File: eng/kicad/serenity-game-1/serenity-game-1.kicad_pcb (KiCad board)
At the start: 2 copper layers, 9 parts, among them U1 PIC16F690-IP

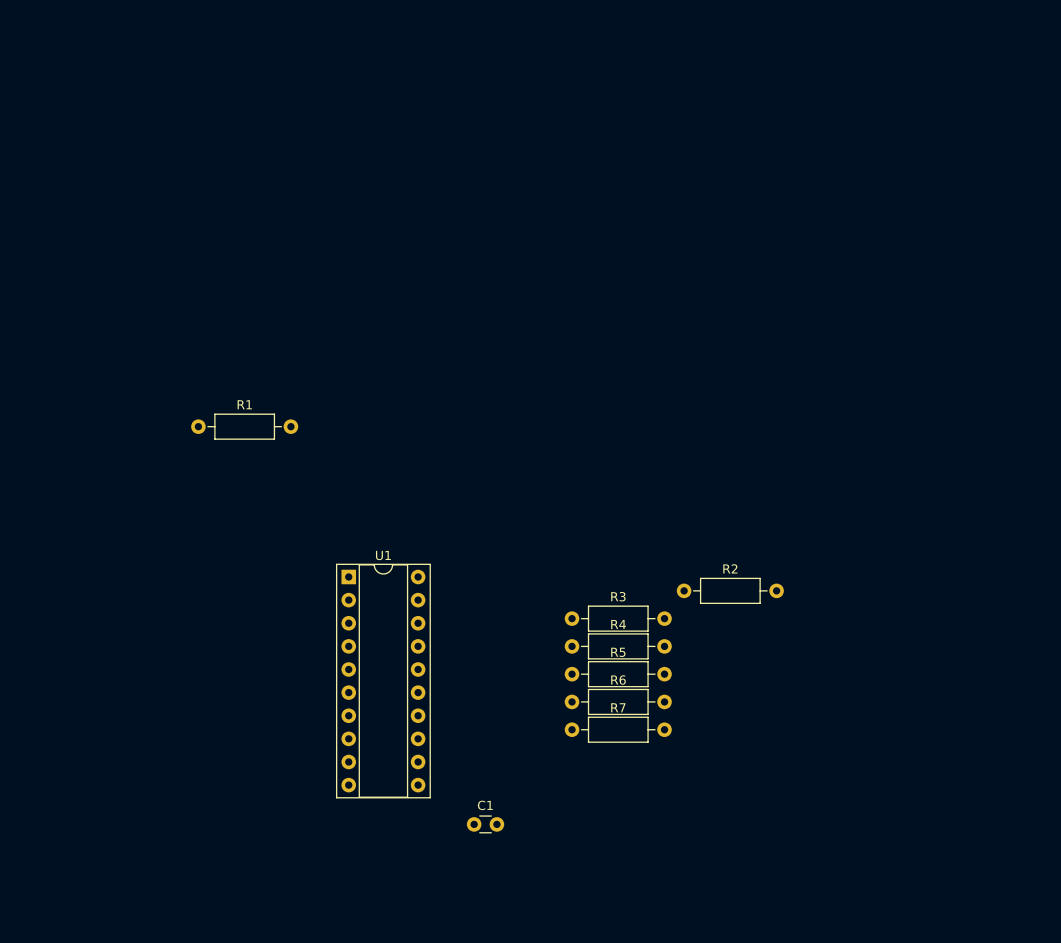
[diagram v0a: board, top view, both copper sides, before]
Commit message: Schematic addition of buttons and labeling of wires (WIP).
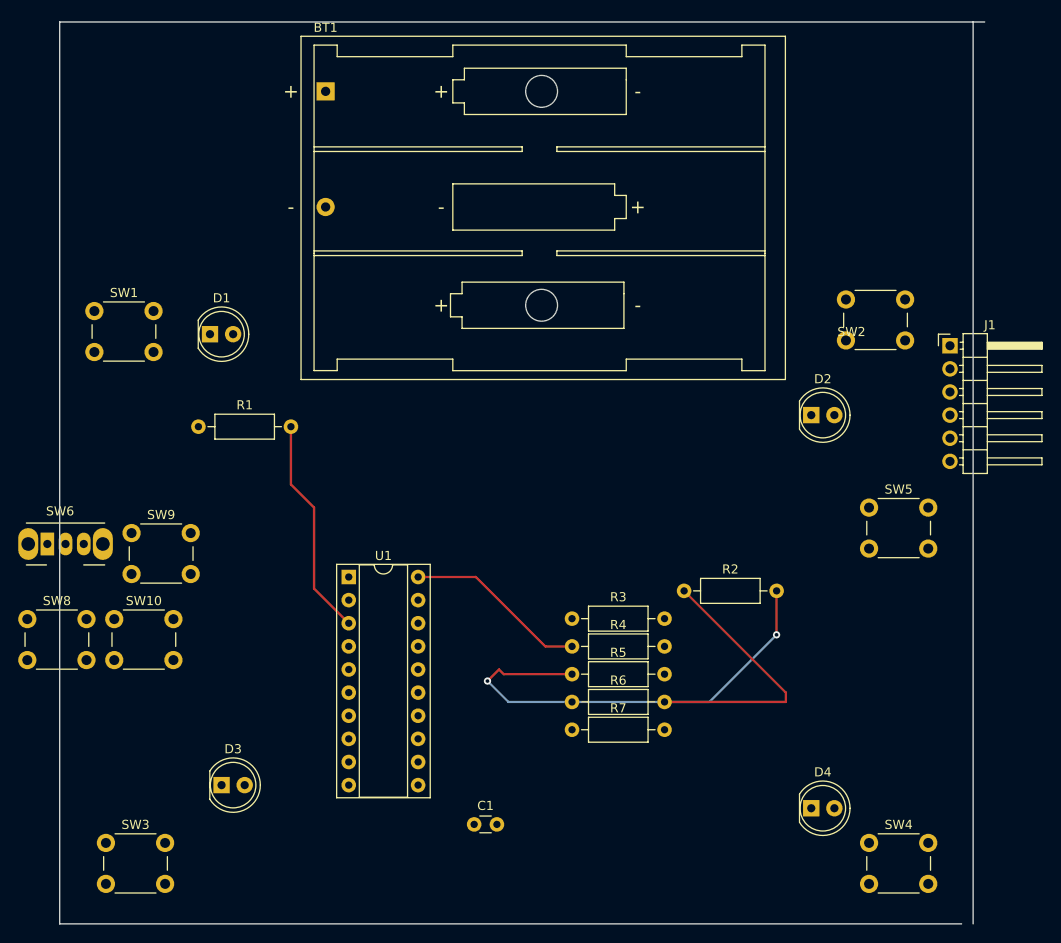
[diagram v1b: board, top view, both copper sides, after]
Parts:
- added BT1: Battery, Battery:BatteryHolder_Keystone_2479_3xAAA, F.Cu at (111.8, 26.7)
- added D1: LED, LED_THT:LED_D5.0mm, F.Cu at (99.1, 53.3)
- added D2: LED, LED_THT:LED_D5.0mm, F.Cu at (165.1, 62.2)
- added D3: LED, LED_THT:LED_D5.0mm, F.Cu at (100.3, 102.9)
- added D4: LED, LED_THT:LED_D5.0mm, F.Cu at (165.1, 105.4)
- added J1: Conn_01x06_Male, Connector_PinHeader_2.54mm:PinHeader_1x06_P2.54mm_Horizontal, F.Cu at (180.3, 54.6)
- added SW1: SW_Push, Button_Switch_THT:SW_PUSH_6mm_H7.3mm, F.Cu at (86.4, 50.8)
- added SW10: SW_Push, Button_Switch_THT:SW_PUSH_6mm_H7.3mm, F.Cu at (88.5, 84.6)
- added SW2: SW_Push, Button_Switch_THT:SW_PUSH_6mm_H7.3mm, F.Cu at (168.9, 49.5)
- added SW3: SW_Push, Button_Switch_THT:SW_PUSH_6mm_H7.3mm, F.Cu at (87.6, 109.2)
- added SW4: SW_Push, Button_Switch_THT:SW_PUSH_6mm_H7.3mm, F.Cu at (171.4, 109.2)
- added SW5: SW_Push, Button_Switch_THT:SW_PUSH_6mm_H7.3mm, F.Cu at (171.4, 72.4)
- added SW6: SW_SPDT, Button_Switch_THT:SW_CuK_OS102011MA1QN1_SPDT_Angled, F.Cu at (81.2, 76.4)
- added SW8: SW_Push, Button_Switch_THT:SW_PUSH_6mm_H7.3mm, F.Cu at (79.0, 84.6)
- added SW9: SW_Push, Button_Switch_THT:SW_PUSH_6mm_H7.3mm, F.Cu at (90.4, 75.2)
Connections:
- C1 pad 1: (no net) -> Net-(C1-Pad1)
- C1 pad 2: (no net) -> Net-(C1-Pad2)
- R1 pad 1: (no net) -> Net-(R1-Pad1)
- R1 pad 2: (no net) -> Net-(R1-Pad2)
- R2 pad 1: (no net) -> Net-(R2-Pad1)
- R2 pad 2: (no net) -> Net-(R2-Pad2)
- R3 pad 1: (no net) -> Net-(R3-Pad1)
- R3 pad 2: (no net) -> Net-(R3-Pad2)
- R4 pad 1: (no net) -> Net-(R4-Pad1)
- R4 pad 2: (no net) -> Net-(R4-Pad2)
- R5 pad 1: (no net) -> Net-(R5-Pad1)
- R5 pad 2: (no net) -> Net-(R5-Pad2)
- R6 pad 1: (no net) -> Net-(R6-Pad1)
- R6 pad 2: (no net) -> Net-(R6-Pad2)
- R7 pad 1: (no net) -> Net-(R7-Pad1)
- R7 pad 2: (no net) -> Net-(R7-Pad2)
- U1 pad 1: (no net) -> Net-(U1-Pad1)
- U1 pad 10: (no net) -> Net-(U1-Pad10)
- U1 pad 11: (no net) -> Net-(U1-Pad11)
- U1 pad 12: (no net) -> Net-(U1-Pad12)
- U1 pad 13: (no net) -> Net-(U1-Pad13)
- U1 pad 14: (no net) -> Net-(U1-Pad14)
- U1 pad 15: (no net) -> Net-(U1-Pad15)
- U1 pad 16: (no net) -> Net-(U1-Pad16)
- U1 pad 17: (no net) -> Net-(U1-Pad17)
- U1 pad 18: (no net) -> Net-(U1-Pad18)
- U1 pad 19: (no net) -> Net-(U1-Pad19)
- U1 pad 2: (no net) -> Net-(U1-Pad2)
- U1 pad 20: (no net) -> Net-(U1-Pad20)
- U1 pad 3: (no net) -> Net-(U1-Pad3)
- U1 pad 4: (no net) -> Net-(U1-Pad4)
- U1 pad 5: (no net) -> /LED2_YELLOW
- U1 pad 6: (no net) -> /LED1_RED
- U1 pad 7: (no net) -> /AUDIO
- U1 pad 8: (no net) -> /LED3_GREEN
- U1 pad 9: (no net) -> /LED4_BLUE
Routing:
- net (no net): track 0.00 -> 125.1 mm, vias 0 -> 2
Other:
- board outline added: 101.6 x 99.1 mm
